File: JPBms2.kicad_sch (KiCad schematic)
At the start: 0 parts

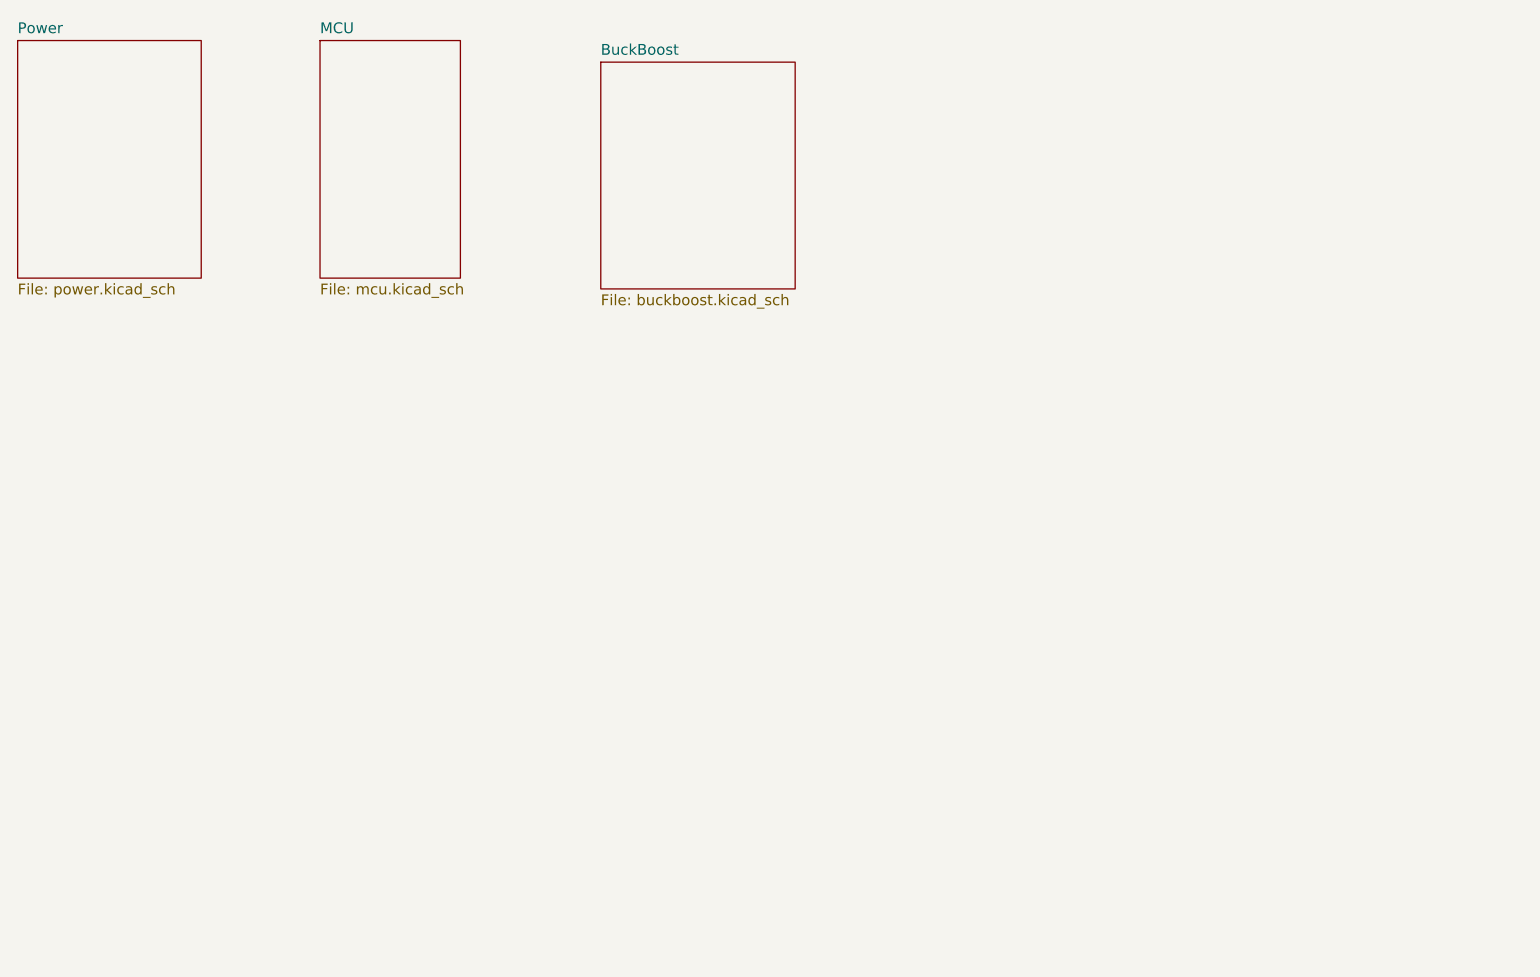
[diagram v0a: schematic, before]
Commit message: Some part selections
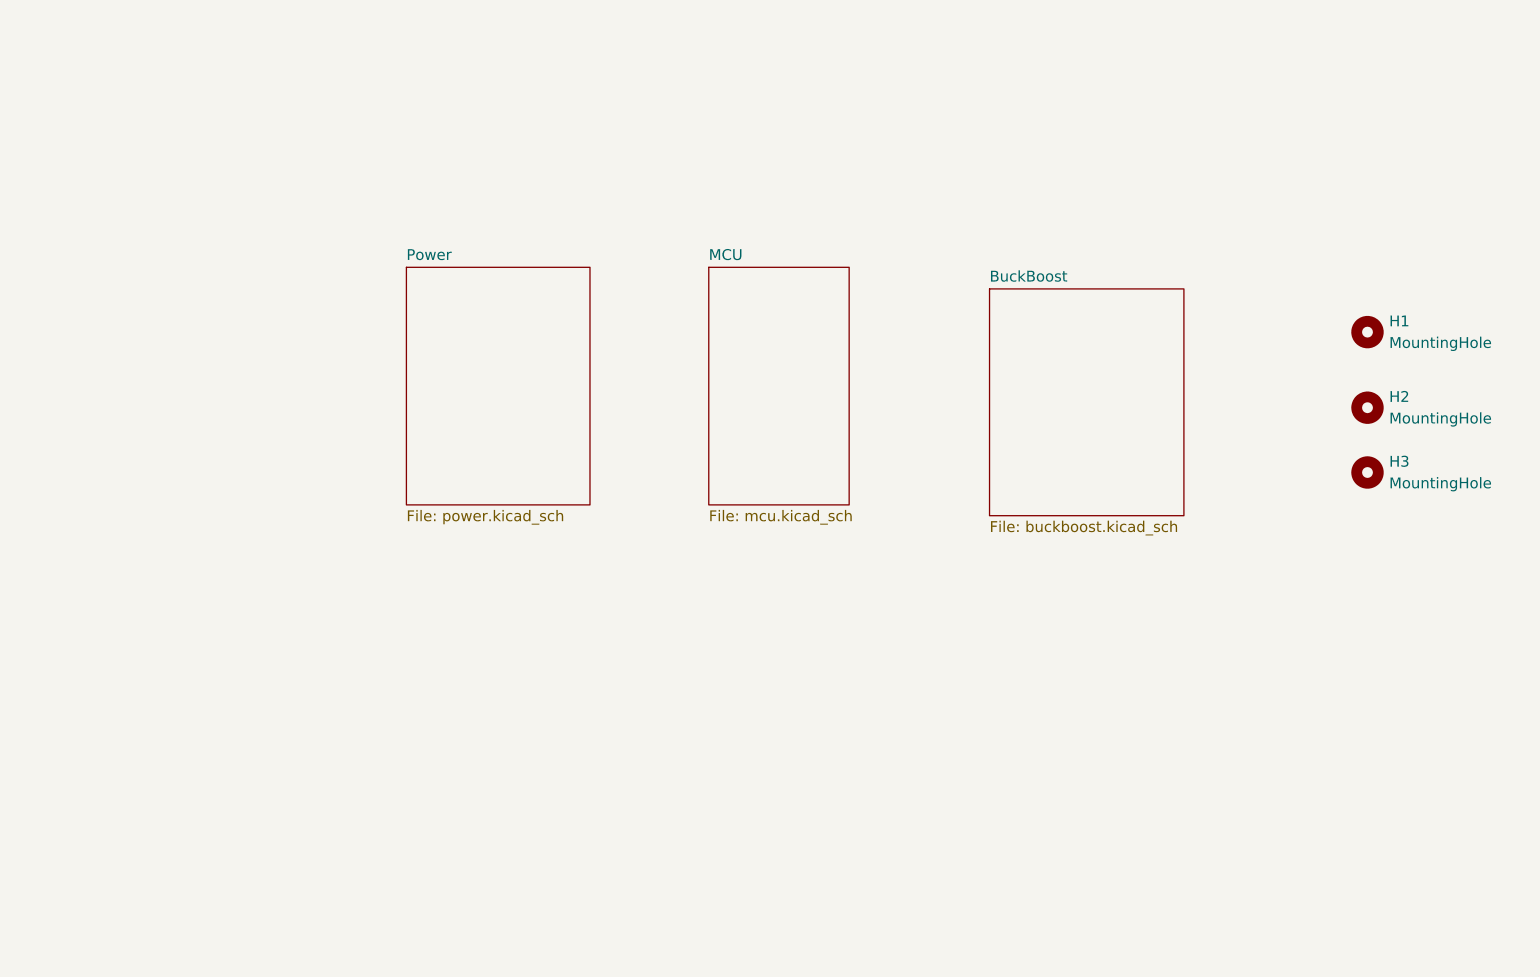
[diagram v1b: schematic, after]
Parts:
- added H1, H2, H3: MountingHole, MountingHole:MountingHole_3.2mm_M3, symbol Mechanical:MountingHole
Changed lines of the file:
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@@
 	(generator_version "8.0")
 	(paper "A4")
+	(symbol
+		(lib_id "Mechanical:MountingHole")
+		(at 181.61 60.96 0)
+		(unit 1)
+		(exclude_from_sim yes)
+		(in_bom no)
+		(on_board yes)
+		(dnp no)
+		(fields_autoplaced yes)
+		(property "Reference" "H2"
+			(at 184.15 59.6899 0)
+			(effects
+				(font
+					(size 1.27 1.27)
+				)
+				(justify left)
+			)
+		)
+		(property "Value" "MountingHole"
+			(at 184.15 62.2299 0)
+			(effects
+				(font
+					(size 1.27 1.27)
+				)
+				(justify left)
+			)
+		)
+		(property "Footprint" "MountingHole:MountingHole_3.2mm_M3"
+			(at 181.61 60.96 0)
+			(effects
+				(font
+					(size 1.27 1.27)
+				)
+				(hide yes)
+			)
+		)
+		(property "Datasheet" "~"
+			(at 181.61 60.96 0)
+			(effects
+				(font
+					(size 1.27 1.27)
+				)
+				(hide yes)
+			)
+		)
+		(property "Description" "Mounting Hole without connection"
+			(at 181.61 60.96 0)
+			(effects
+				(font
+					(size 1.27 1.27)
+				)
+				(hide yes)
+			)
+		)
+		(instances
+			(project "JPBms2"
+				(path "/d86e471c-a8be-422d-a5d1-5a4699b7b766"
+					(reference "H2")
+					(unit 1)
+				)
+			)
+		)
+	)
+	(symbol
+		(lib_id "Mechanical:MountingHole")
+		(at 181.61 68.58 0)
+		(unit 1)
+		(exclude_from_sim yes)
+		(in_bom no)
+		(on_board yes)
+		(dnp no)
+		(fields_autoplaced yes)
+		(property "Reference" "H3"
+			(at 184.15 67.3099 0)
+			(effects
+				(font
+					(size 1.27 1.27)
+				)
+				(justify left)
+			)
+		)
+		(property "Value" "MountingHole"
+			(at 184.15 69.8499 0)
+			(effects
+				(font
+					(size 1.27 1.27)
+				)
+				(justify left)
+			)
+		)
+		(property "Footprint" "MountingHole:MountingHole_3.2mm_M3"
+			(at 181.61 68.58 0)
+			(effects
+				(font
+					(size 1.27 1.27)
+				)
+				(hide yes)
+			)
+		)
+		(property "Datasheet" "~"
+			(at 181.61 68.58 0)
+			(effects
+				(font
+					(size 1.27 1.27)
+				)
+				(hide yes)
+			)
+		)
+		(property "Description" "Mounting Hole without connection"
+			(at 181.61 68.58 0)
+			(effects
+				(font
+					(size 1.27 1.27)
+				)
+				(hide yes)
+			)
+		)
+		(instances
+			(project "JPBms2"
+				(path "/d86e471c-a8be-422d-a5d1-5a4699b7b766"
+					(reference "H3")
+					(unit 1)
+				)
+			)
+		)
+	)
+	(symbol
+		(lib_id "Mechanical:MountingHole")
+		(at 181.61 52.07 0)
+		(unit 1)
+		(exclude_from_sim yes)
+		(in_bom no)
+		(on_board yes)
+		(dnp no)
+		(fields_autoplaced yes)
+		(property "Reference" "H1"
+			(at 184.15 50.7999 0)
+			(effects
+				(font
+					(size 1.27 1.27)
+				)
+				(justify left)
+			)
+		)
+		(property "Value" "MountingHole"
+			(at 184.15 53.3399 0)
+			(effects
+				(font
+					(size 1.27 1.27)
+				)
+				(justify left)
+			)
+		)
+		(property "Footprint" "MountingHole:MountingHole_3.2mm_M3"
+			(at 181.61 52.07 0)
+			(effects
+				(font
+					(size 1.27 1.27)
+				)
+				(hide yes)
+			)
+		)
+		(property "Datasheet" "~"
+			(at 181.61 52.07 0)
+			(effects
+				(font
+					(size 1.27 1.27)
+				)
+				(hide yes)
+			)
+		)
+		(property "Description" "Mounting Hole without connection"
+			(at 181.61 52.07 0)
+			(effects
+				(font
+					(size 1.27 1.27)
+				)
+				(hide yes)
+			)
+		)
+		(instances
+			(project "JPBms2"
+				(path "/d86e471c-a8be-422d-a5d1-5a4699b7b766"
+					(reference "H1")
+					(unit 1)
+				)
+			)
+		)
+	)
 	(sheet
-		(at 91.44 20.32)
+		(at 137.16 46.99)
 		(size 22.86 26.67)
 		(fields_autoplaced yes)
@@
 		)
 		(property "Sheetname" "BuckBoost"
-			(at 91.44 19.6084 0)
+			(at 137.16 46.2784 0)
 			(effects
 				(font
@@
 		)
 		(property "Sheetfile" "buckboost.kicad_sch"
-			(at 91.44 47.5746 0)
+			(at 137.16 74.2446 0)
 			(effects
 				(font
@@
 	)
 	(sheet
-		(at 58.42 17.78)
+		(at 104.14 44.45)
 		(size 16.51 27.94)
 		(fields_autoplaced yes)
@@
 		)
 		(property "Sheetname" "MCU"
-			(at 58.42 17.0684 0)
+			(at 104.14 43.7384 0)
 			(effects
 				(font
@@
 		)
 		(property "Sheetfile" "mcu.kicad_sch"
-			(at 58.42 46.3046 0)
+			(at 104.14 72.9746 0)
 			(effects
 				(font
@@
 	)
 	(sheet
-		(at 22.86 17.78)
+		(at 68.58 44.45)
 		(size 21.59 27.94)
 		(fields_autoplaced yes)
@@
 		)
 		(property "Sheetname" "Power"
-			(at 22.86 17.0684 0)
+			(at 68.58 43.7384 0)
 			(effects
 				(font
@@
 		)
 		(property "Sheetfile" "power.kicad_sch"
-			(at 22.86 46.3046 0)
-			(effects
-				(font
+			(at 68.58 72.9746 0)
+			(effects
+				(font

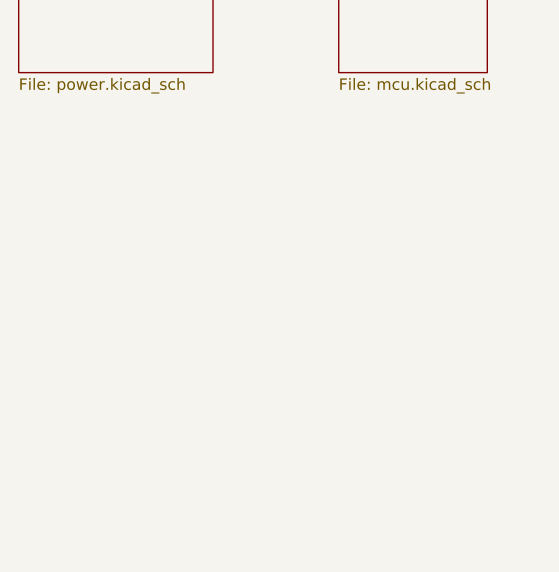
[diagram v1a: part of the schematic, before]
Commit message: Adding simple balance circuits
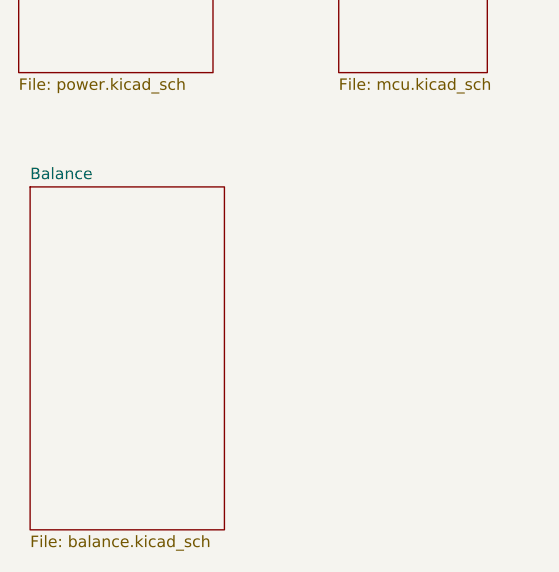
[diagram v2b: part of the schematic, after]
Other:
- added sheet Balance (balance.kicad_sch)
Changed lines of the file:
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@@
+	)
+	(sheet
+		(at 69.85 85.09)
+		(size 21.59 38.1)
+		(fields_autoplaced yes)
+		(stroke
+			(width 0.1524)
+			(type solid)
+		)
+		(fill
+			(color 0 0 0 0.0000)
+		)
+		(property "Sheetname" "Balance"
+			(at 69.85 84.3784 0)
+			(effects
+				(font
+					(size 1.27 1.27)
+				)
+				(justify left bottom)
+			)
+		)
+		(property "Sheetfile" "balance.kicad_sch"
+			(at 69.85 123.7746 0)
+			(effects
+				(font
+					(size 1.27 1.27)
+				)
+				(justify left top)
+			)
+		)
+		(instances
+			(project "JPBms2"
+				(path "/d86e471c-a8be-422d-a5d1-5a4699b7b766"
+					(page "5")
+				)
+			)
+		)
 	)
 	(sheet

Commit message: notes
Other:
- added sheet ADC (adc.kicad_sch)
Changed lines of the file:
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@@
+	)
+	(sheet
+		(at 107.95 85.09)
+		(size 16.51 38.1)
+		(fields_autoplaced yes)
+		(stroke
+			(width 0.1524)
+			(type solid)
+		)
+		(fill
+			(color 0 0 0 0.0000)
+		)
+		(property "Sheetname" "ADC"
+			(at 107.95 84.3784 0)
+			(effects
+				(font
+					(size 1.27 1.27)
+				)
+				(justify left bottom)
+			)
+		)
+		(property "Sheetfile" "adc.kicad_sch"
+			(at 107.95 123.7746 0)
+			(effects
+				(font
+					(size 1.27 1.27)
+				)
+				(justify left top)
+			)
+		)
+		(instances
+			(project "JPBms2"
+				(path "/d86e471c-a8be-422d-a5d1-5a4699b7b766"
+					(page "6")
+				)
+			)
+		)
 	)
 	(sheet

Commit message: Layout
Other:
- moved on the sheet: H1, H2, H3
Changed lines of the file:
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@@
 	(symbol
 		(lib_id "Mechanical:MountingHole")
-		(at 181.61 60.96 0)
+		(at 189.23 67.31 90)
 		(unit 1)
 		(exclude_from_sim yes)
@@
 		(fields_autoplaced yes)
 		(property "Reference" "H2"
-			(at 184.15 59.6899 0)
+			(at 187.9599 64.77 0)
 			(effects
 				(font
@@
 		)
 		(property "Value" "MountingHole"
-			(at 184.15 62.2299 0)
+			(at 190.4999 64.77 0)
 			(effects
 				(font
@@
 		)
 		(property "Footprint" "MountingHole:MountingHole_3.2mm_M3"
-			(at 181.61 60.96 0)
+			(at 189.23 67.31 0)
 			(effects
 				(font
@@
 		)
 		(property "Datasheet" "~"
-			(at 181.61 60.96 0)
+			(at 189.23 67.31 0)
 			(effects
 				(font
@@
 		)
 		(property "Description" "Mounting Hole without connection"
-			(at 181.61 60.96 0)
+			(at 189.23 67.31 0)
 			(effects
 				(font
@@
 		)
 		(property "Sim.Device" ""
-			(at 181.61 60.96 0)
+			(at 189.23 67.31 0)
 			(effects
 				(font
@@
 		)
 		(property "Sim.Pins" ""
-			(at 181.61 60.96 0)
+			(at 189.23 67.31 0)
 			(effects
 				(font
@@
 		)
 		(property "Tolerance" ""
-			(at 181.61 60.96 0)
+			(at 189.23 67.31 0)
 			(effects
 				(font
@@
 	(symbol
 		(lib_id "Mechanical:MountingHole")
-		(at 181.61 68.58 0)
+		(at 196.85 67.31 90)
 		(unit 1)
 		(exclude_from_sim yes)
@@
 		(fields_autoplaced yes)
 		(property "Reference" "H3"
-			(at 184.15 67.3099 0)
+			(at 195.5799 64.77 0)
 			(effects
 				(font
@@
 		)
 		(property "Value" "MountingHole"
-			(at 184.15 69.8499 0)
+			(at 198.1199 64.77 0)
 			(effects
 				(font
@@
 		)
 		(property "Footprint" "MountingHole:MountingHole_3.2mm_M3"
-			(at 181.61 68.58 0)
+			(at 196.85 67.31 0)
 			(effects
 				(font
@@
 		)
 		(property "Datasheet" "~"
-			(at 181.61 68.58 0)
+			(at 196.85 67.31 0)
 			(effects
 				(font
@@
 		)
 		(property "Description" "Mounting Hole without connection"
-			(at 181.61 68.58 0)
+			(at 196.85 67.31 0)
 			(effects
 				(font
@@
 		)
 		(property "Sim.Device" ""
-			(at 181.61 68.58 0)
+			(at 196.85 67.31 0)
 			(effects
 				(font
@@
 		)
 		(property "Sim.Pins" ""
-			(at 181.61 68.58 0)
+			(at 196.85 67.31 0)
 			(effects
 				(font
@@
 		)
 		(property "Tolerance" ""
-			(at 181.61 68.58 0)
+			(at 196.85 67.31 0)
 			(effects
 				(font
@@
 	(symbol
 		(lib_id "Mechanical:MountingHole")
-		(at 181.61 52.07 0)
+		(at 180.34 67.31 90)
 		(unit 1)
 		(exclude_from_sim yes)
@@
 		(fields_autoplaced yes)
 		(property "Reference" "H1"
-			(at 184.15 50.7999 0)
+			(at 179.0699 64.77 0)
 			(effects
 				(font
@@
 		)
 		(property "Value" "MountingHole"
-			(at 184.15 53.3399 0)
+			(at 181.6099 64.77 0)
 			(effects
 				(font
@@
 		)
 		(property "Footprint" "MountingHole:MountingHole_3.2mm_M3"
-			(at 181.61 52.07 0)
+			(at 180.34 67.31 0)
 			(effects
 				(font
@@
 		)
 		(property "Datasheet" "~"
-			(at 181.61 52.07 0)
+			(at 180.34 67.31 0)
 			(effects
 				(font
@@
 		)
 		(property "Description" "Mounting Hole without connection"
-			(at 181.61 52.07 0)
+			(at 180.34 67.31 0)
 			(effects
 				(font
@@
 		)
 		(property "Sim.Device" ""
-			(at 181.61 52.07 0)
+			(at 180.34 67.31 0)
 			(effects
 				(font
@@
 		)
 		(property "Sim.Pins" ""
-			(at 181.61 52.07 0)
+			(at 180.34 67.31 0)
 			(effects
 				(font
@@
 		)
 		(property "Tolerance" ""
-			(at 181.61 52.07 0)
-			(effects
-				(font
+			(at 180.34 67.31 0)
+			(effects
+				(font
